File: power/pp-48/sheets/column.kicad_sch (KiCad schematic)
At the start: 55 parts, among them J101 NODE 19V, J102 FRONT PANEL, J103 AUX, Q101 BSC070N10NS5, Q102 2N7002, Q103 2N7002, Q104 2N7002, Q105 2N7002, U101 LM5069MM-2, U102 INA238AIDGSR, U103 74LVC1G74, U104 ADC121C027CIMK, U105 TCA9535PWR, U106 TLP176AM, U107 TLP176AM, U108 TLP291

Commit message: pp-48: placement draft for review (2 columns, 50 x 72 mm, unrouted): tools/place.py one column table copied by translation, front end under the module, tall parts on B; DG128 footprint; cable-side NODE cap dropped, J1 pin 2 = +19 V under S4; handoff
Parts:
- removed C108: 2.2u 50V, Capacitor_SMD:C_1210_3225Metric, symbol Device:C
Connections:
- net GND: now also J101.1 (Pin_1); no longer J101.2 (Pin_2)
- net NODE: now also J101.2 (Pin_2); no longer J101.1 (Pin_1)

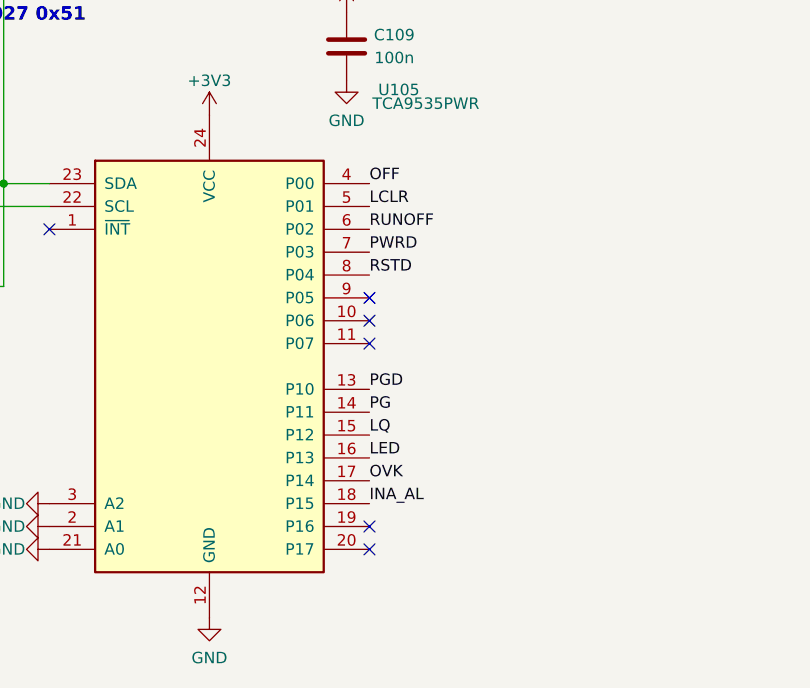
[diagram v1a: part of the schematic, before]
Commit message: pp-48: placement rework by signal flow (expander in the middle, pins reassigned by board side; enable chain and latch under the LM5069; ID ADC, RUN FET, pull-ups around the socket; photoMOS / opto back lower left on B); column 1 rerouted and copied, 0 unconnected; gndstitch.py ties floating GND pour islands to In1; handoff
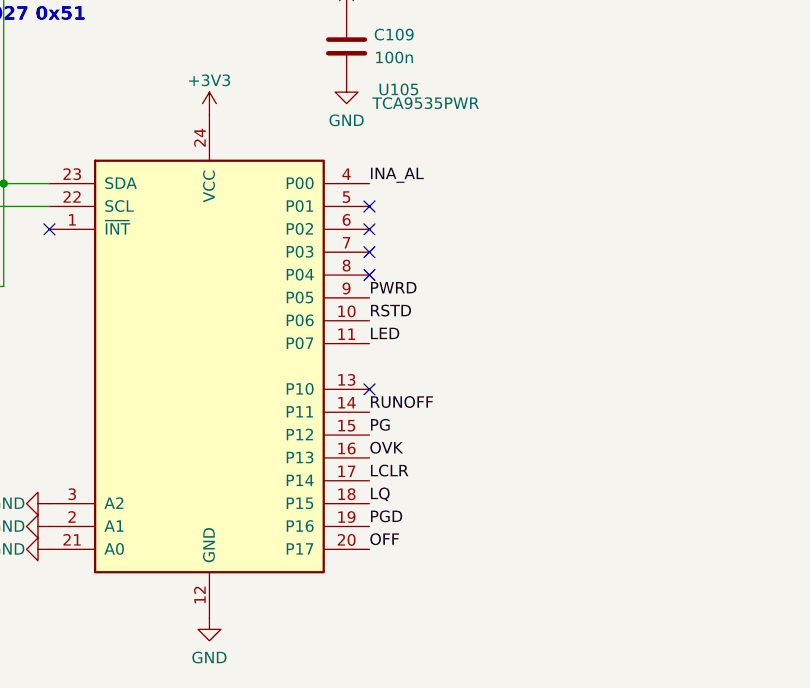
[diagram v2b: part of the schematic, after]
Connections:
- net INA_AL: now also U105.4 (P00); no longer U105.18 (P15)
- net LCLR: now also U105.17 (P14); no longer U105.5 (P01)
- net LED: now also U105.11 (P07); no longer U105.16 (P13)
- net LQ: now also U105.18 (P15); no longer U105.15 (P12)
- net OFF: now also U105.20 (P17); no longer U105.4 (P00)
- net OVK: now also U105.16 (P13); no longer U105.17 (P14)
- net PG: now also U105.15 (P12); no longer U105.14 (P11)
- net PGD: now also U105.19 (P16); no longer U105.13 (P10)
- net PWRD: now also U105.9 (P05); no longer U105.7 (P03)
- net RSTD: now also U105.10 (P06); no longer U105.8 (P04)
- net RUNOFF: now also U105.14 (P11); no longer U105.6 (P02)
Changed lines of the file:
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@@
 	)
 	(no_connect
-		(at 119.38 220.98)
+		(at 119.38 210.82)
 	)
 	(no_connect
-		(at 119.38 223.52)
+		(at 119.38 213.36)
 	)
 	(no_connect
-		(at 119.38 226.06)
+		(at 119.38 215.9)
 	)
 	(no_connect
-		(at 119.38 246.38)
+		(at 119.38 218.44)
 	)
 	(no_connect
-		(at 119.38 248.92)
+		(at 119.38 231.14)
 	)
 	(hierarchical_label "SDA"
@@
 		)
 	)
-	(label "OFF"
+	(label "INA_AL"
 		(at 119.38 208.28 0)
 		(effects
@@
 		)
 	)
-	(label "LCLR"
-		(at 119.38 210.82 0)
+	(label "PWRD"
+		(at 119.38 220.98 0)
 		(effects
 			(font
@@
 		)
 	)
-	(label "RUNOFF"
-		(at 119.38 213.36 0)
+	(label "RSTD"
+		(at 119.38 223.52 0)
 		(effects
 			(font
@@
 		)
 	)
-	(label "PWRD"
-		(at 119.38 215.9 0)
+	(label "LED"
+		(at 119.38 226.06 0)
 		(effects
 			(font
@@
 		)
 	)
-	(label "RSTD"
-		(at 119.38 218.44 0)
+	(label "RUNOFF"
+		(at 119.38 233.68 0)
 		(effects
 			(font
@@
 		)
 	)
-	(label "PGD"
-		(at 119.38 231.14 0)
+	(label "PG"
+		(at 119.38 236.22 0)
 		(effects
 			(font
@@
 		)
 	)
-	(label "PG"
-		(at 119.38 233.68 0)
+	(label "OVK"
+		(at 119.38 238.76 0)
 		(effects
 			(font
@@
 		)
 	)
-	(label "LQ"
-		(at 119.38 236.22 0)
+	(label "LCLR"
+		(at 119.38 241.3 0)
 		(effects
 			(font
@@
 		)
 	)
-	(label "LED"
-		(at 119.38 238.76 0)
+	(label "LQ"
+		(at 119.38 243.84 0)
 		(effects
 			(font
@@
 		)
 	)
-	(label "OVK"
-		(at 119.38 241.3 0)
+	(label "PGD"
+		(at 119.38 246.38 0)
 		(effects
 			(font
@@
 		)
 	)
-	(label "INA_AL"
-		(at 119.38 243.84 0)
+	(label "OFF"
+		(at 119.38 248.92 0)
 		(effects
 			(font
@@
 			)
 		)
-		(property "Description" "slot GPIO, address 0x20 (A0-A2 GND); P0 out: OFF LCLR RUNOFF PWRD RSTD, P1 in: PGD PG LQ LED OVK INA_AL; INT unused (polled)"
+		(property "Description" "slot GPIO, address 0x20 (A0-A2 GND); pins by board side: P00 INA_AL in, P05 PWRD out, P06 RSTD out, P07 LED in; P17 OFF out, P16 PGD in, P15 LQ in, P14 LCLR out, P13 OVK in, P12 PG in, P11 RUNOFF out; INT unused (polled)"
 			(at 101.6 228.6 0)
 			(hide yes)

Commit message: pp-48: slot OVLO 124k / 4.99k (64.6 V, 60.9-68.5 V worst case, below the module's 67.5 V nominally); D1 SMBJ60A kept (breakdown >= 66.7 V, SMBJ64A clamps at 103 V); values synced to the board, DRC unchanged; ADR 0003 items closed
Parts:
- R105: value 240k -> 124k
- R106: value 10k -> 4.99k; LCSC C25744 -> (none)
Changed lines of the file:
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@@
 			)
 		)
-		(property "Value" "240k"
+		(property "Value" "124k"
 			(at 100.806 71.12 0)
 			(show_name no)
@@
 			)
 		)
-		(property "Description" "OVLO: off 62.5 V, back at 57.5 V (to raise to ~66-68 V, ADR 0003)"
+		(property "Description" "OVLO: off 64.6 V (60.9-68.5 V over 2.4-2.6 V and 1 %), back on ~2.6 V lower (12-30 uA x 124k); module trips at 67.5 V"
 			(at 96.52 69.85 0)
 			(hide yes)
@@
 			)
 		)
-		(property "Value" "10k"
-			(at 100.306 81.28 0)
+		(property "Value" "4.99k"
+			(at 101.306 81.28 0)
 			(show_name no)
 			(do_not_autoplace no)
@@
 			)
 		)
-		(property "LCSC" "C25744"
+		(property "LCSC" ""
 			(at 96.52 80.01 0)
 			(hide yes)
@@
 			)
 		)
-		(property "Description" "slot output clamp (cable inductance on a cut); 60 V standoff vs the 60 V top of range: open"
+		(property "Description" "slot output clamp: 60 V standoff = top of the bus range, breakdown >= 66.7 V; SMBJ64A would clamp at 103 V, over the 100 V FET and module"
 			(at 142.24 48.26 0)
 			(hide yes)

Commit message: pp-48: slot latch also set by the INA238 ALERT (straight onto OVK, R25 gone) and by PGOOD loss with arm-on-first-PGOOD blanking (U10 set while PG and PGD high via Q8 / Q9, cleared while PGD low; trip FET Q6; DISARM on expander P10 via Q7 around RUNOFF); arm cluster on F at the left edge, U3 OVK / CLRN escape vias in route_hand.py; column 1 rerouted and copied, solid GND on starved pads, silk; DRC 5 excluded core-side ends (exclusions re-keyed), 0 unconnected, 0 parity; ADR 0003 items closed, handoff
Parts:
- removed R125: 10k, Resistor_SMD:R_0402_1005Metric, symbol Device:R
- added C112: 100n, Capacitor_SMD:C_0402_1005Metric, symbol Device:C
- added Q106, Q107, Q108, Q109: 2N7002, Package_TO_SOT_SMD:SOT-23, symbol Transistor_FET:2N7002
- added R128, R129: 100k, Resistor_SMD:R_0402_1005Metric, symbol Device:R
- added U110: 74LVC1G74, Package_SO:VSSOP-8_2.3x2mm_P0.5mm, symbol 74xGxx:74AUC1G74
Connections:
- net +3V3: now also C112.1, R128.1, U110.8 (VCC)
- net GND: now also C112.2, Q107.2 (S), Q109.2 (S), R129.2, U110.1 (C), U110.2 (D), U110.4 (GND)
- net OVK: now also U102.3 (~{Alert}), Q106.3 (D)
- net PG: now also Q106.2 (S), Q108.1 (G)
- net PGD: now also Q107.3 (D), Q109.1 (G), U110.6 (~{CLR})
- net DISARM: now reaches U105.13 (P10)
- net DISARM: now also Q107.1 (G), R129.1
- net INA_AL: no longer names the net of U105.4 (P00)
- net INA_AL: no longer U102.3 (~{Alert})
- new net ARM: Q106.1 (G), U110.5 (Q)
- new net ARMS_M: Q108.2 (S), Q109.3 (D)
- new net ARMS_N: Q108.3 (D), R128.2, U110.7 (~{PRE})
- no-connect marks 7 -> 8

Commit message: pp-48: TVS polarity fix (slot clamp SMBJ60A and bus TVS SMDJ60A are unidirectional: cathode pad 1 now on OUT / VIN, symbol Device:D_Zener; they had pad 1 on GND and would have shorted the rail); Input resistors renumbered R33-R38 (collided with the 3V3 buck's R3-R8); handoff notes the same bug in pp-48-2s
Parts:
- D101: symbol Device:D_TVS -> Device:D_Zener
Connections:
- net GND: now also D101.2 (A); no longer D101.1 (A1)
- net OUT: now also D101.1 (K); no longer D101.2 (A2)
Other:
- moved on the sheet: D101
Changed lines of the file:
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@@
 	)
 	(symbol
-		(lib_id "Device:D_TVS")
-		(at 142.24 48.26 90)
+		(lib_id "Device:D_Zener")
+		(at 142.24 48.26 270)
 		(unit 1)
 		(body_style 1)
@@
 			)
 		)
-		(property "Description" "slot output clamp: 60 V standoff = top of the bus range, breakdown >= 66.7 V; SMBJ64A would clamp at 103 V, over the 100 V FET and module"
+		(property "Description" "slot output clamp, unidirectional: cathode (pad 1) on OUT; 60 V standoff = top of the bus range, breakdown >= 66.7 V; SMBJ64A would clamp at 103 V, over the 100 V FET and module"
 			(at 142.24 48.26 0)
 			(hide yes)
